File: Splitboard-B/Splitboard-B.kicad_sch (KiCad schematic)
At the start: 86 parts, among them J1 USB_C_Receptacle, K1 KEYSW, K10 KEYSW, K11 KEYSW, K12 KEYSW, K13 KEYSW, K14 KEYSW, K15 KEYSW, K16 KEYSW, K17 KEYSW, K18 KEYSW, K19 KEYSW, K2 KEYSW, K20 KEYSW, K21 KEYSW, K22 KEYSW, K23 KEYSW, K24 KEYSW, K25 KEYSW, K26 KEYSW, K27 KEYSW, K28 KEYSW, K29 KEYSW, K3 KEYSW, K30 KEYSW, K31 KEYSW, K32 KEYSW, K33 KEYSW, K34 KEYSW, K35 KEYSW, K36 KEYSW, K37 KEYSW, K38 KEYSW, K4 KEYSW, K5 KEYSW, K6 KEYSW, K7 KEYSW, K8 KEYSW, K9 KEYSW, SW1 RotaryEncoder, U1 MCP23018-E{slash}SP, U3 CR2013-MI2120

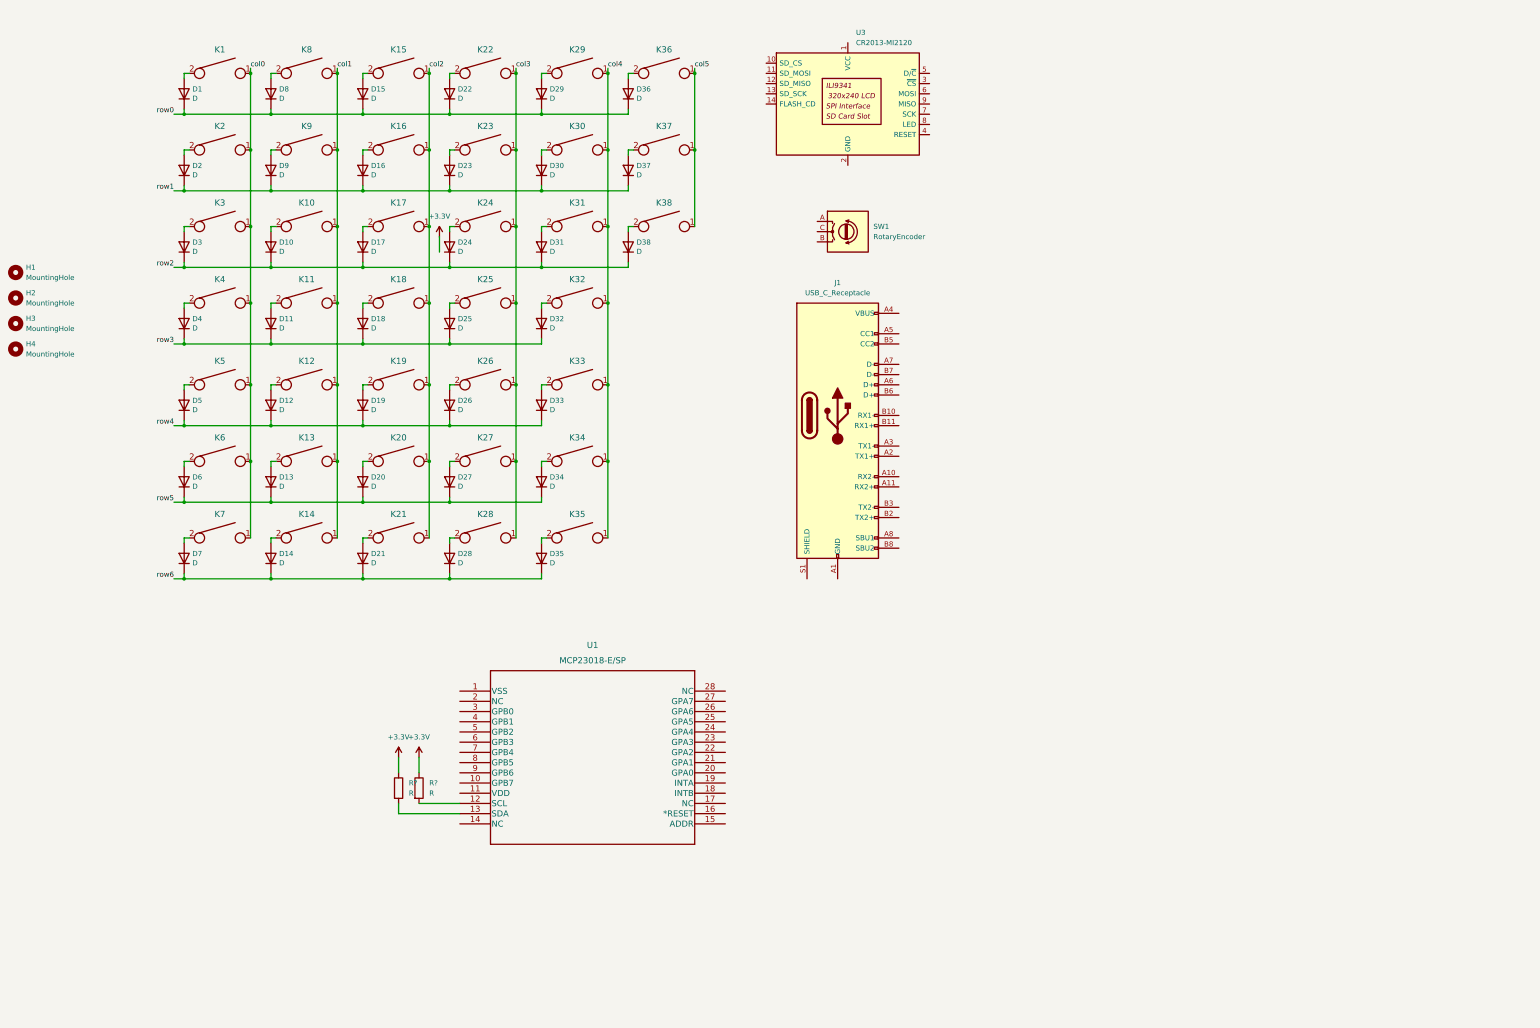
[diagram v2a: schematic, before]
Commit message: Schematic changes, linked both boards under a new project
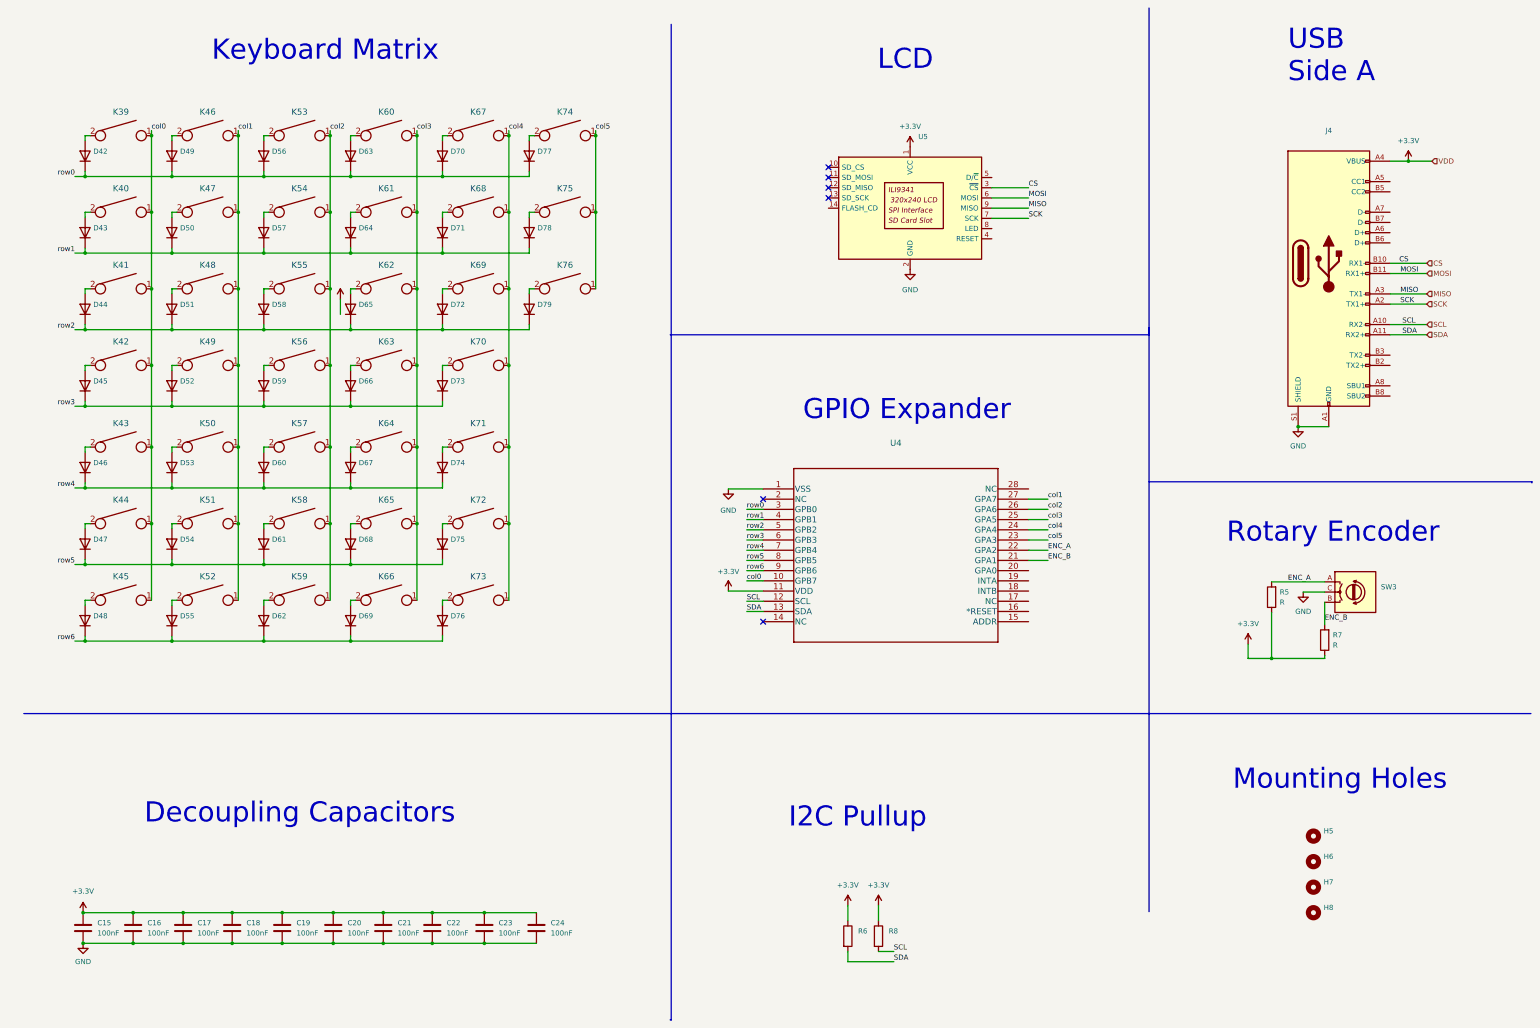
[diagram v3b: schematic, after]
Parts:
- removed D1, D10, D11, D12, D13, D14, D15, D16, D17, D18, D19, D2, D20, D21, D22, D23, D24, D25, D26, D27, D28, D29, D3, D30, D31, D32, D33, D34, D35, D36, D37, D38, D4, D5, D6, D7, D8, D9: D, Diode_SMD:D_SOD-123, symbol KBT1-rescue:D-Device
- removed H1, H2, H3, H4: MountingHole, MountingHole:MountingHole_2.7mm, symbol Mechanical:MountingHole
- removed J1: USB_C_Receptacle, USB_C_Receptacle_GCT_USB4085, symbol Connector:USB_C_Receptacle
- removed K1, K10, K11, K12, K13, K14, K15, K16, K17, K18, K19, K2, K20, K21, K22, K23, K24, K25, K26, K27, K28, K29, K3, K30, K31, K32, K33, K34, K35, K36, K37, K38, K4, K5, K6, K7, K8, K9: KEYSW, 6:SW_Hotswap_Kailh_MX_plated, symbol KBT1-rescue:KEYSW-keyboard_parts
- removed R? (x2): R, symbol Device:R
- removed SW1: RotaryEncoder, Rotary_Encoder:RotaryEncoder_Alps_EC12E_Vertical_H20mm, symbol Device:RotaryEncoder
- removed U3: CR2013-MI2120, Display:CR2013-MI2120, symbol Driver_Display:CR2013-MI2120
- added C15, C16, C17, C18, C19, C20, C21, C22, C23, C24: 100nF, symbol Device:C
- added D42, D43, D44, D45, D46, D47, D48, D49, D50, D51, D52, D53, D54, D55, D56, D57, D58, D59, D60, D61, D62, D63, D64, D65, D66, D67, D68, D69, D70, D71, D72, D73, D74, D75, D76, D77, D78, D79: (no value), symbol KBT1-rescue:D-Device
- added H5, H6, H7, H8: (no value), symbol Mechanical:MountingHole
- added J4: (no value), symbol Connector:USB_C_Receptacle
- added K39, K40, K41, K42, K43, K44, K45, K46, K47, K48, K49, K50, K51, K52, K53, K54, K55, K56, K57, K58, K59, K60, K61, K62, K63, K64, K65, K66, K67, K68, K69, K70, K71, K72, K73, K74, K75, K76: (no value), symbol KBT1-rescue:KEYSW-keyboard_parts
- added R5, R7: R, symbol Device:R
- added R6, R8: ~, symbol Device:R
- added SW3: (no value), symbol Device:RotaryEncoder
- added U5: (no value), symbol Driver_Display:CR2013-MI2120
- U4: renamed from U1; value MCP23018-E/SP -> (none); footprint 6:MCP23018-E&slash_SP -> (none)
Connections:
- net +3.3V: now also U4.11 (VDD), C15.1, C16.1, C17.1, C18.1, C19.1, C20.1, C21.1, C22.1, C23.1, C24.1, J4.A4 (VBUS), J4.A9 (VBUS), J4.B4 (VBUS), J4.B9 (VBUS), R5.1, R6.1, R7.1, R8.1, U5.1 (VCC)
- net col0: now also U4.10 (GPB7), K39.1, K40.1, K41.1, K42.1, K43.1, K44.1, K45.1
- net col1: now also U4.27 (GPA7), K46.1, K47.1, K48.1, K49.1, K50.1, K51.1, K52.1
- net col2: now also U4.26 (GPA6), K53.1, K54.1, K55.1, K56.1, K57.1, K58.1, K59.1
- net col3: now also U4.25 (GPA5), K60.1, K61.1, K62.1, K63.1, K64.1, K65.1, K66.1
- net col4: now also U4.24 (GPA4), K67.1, K68.1, K69.1, K70.1, K71.1, K72.1, K73.1
- net col5: now also U4.23 (GPA3), K74.1, K75.1, K76.1
- net row0: now also U4.3 (GPB0), D42.1 (K), D49.1 (K), D56.1 (K), D63.1 (K), D70.1 (K), D77.1 (K)
- net row1: now also U4.4 (GPB1), D43.1 (K), D50.1 (K), D57.1 (K), D64.1 (K), D71.1 (K), D78.1 (K)
- net row2: now also U4.5 (GPB2), D44.1 (K), D51.1 (K), D58.1 (K), D65.1 (K), D72.1 (K), D79.1 (K)
- net row3: now also U4.6 (GPB3), D45.1 (K), D52.1 (K), D59.1 (K), D66.1 (K), D73.1 (K)
- net row4: now also U4.7 (GPB4), D46.1 (K), D53.1 (K), D60.1 (K), D67.1 (K), D74.1 (K)
- net row5: now also U4.8 (GPB5), D47.1 (K), D54.1 (K), D61.1 (K), D68.1 (K), D75.1 (K)
- net row6: now also U4.9 (GPB6), D48.1 (K), D55.1 (K), D62.1 (K), D69.1 (K), D76.1 (K)
- net GND: now reaches U4.1 (VSS)
- net GND: now also C15.2, C16.2, C17.2, C18.2, C19.2, C20.2, C21.2, C22.2, C23.2, C24.2, J4.A1 (GND), J4.A12 (GND), J4.B1 (GND), J4.B12 (GND), J4.S1 (SHIELD), SW3.C, U5.2 (GND)
- net SCL: now reaches U4.12 (SCL)
- net SCL: now also J4.A10 (RX2-), R8.2
- net SDA: now reaches U4.13 (SDA)
- net SDA: now also J4.A11 (RX2+), R6.2
- net ENC_B: now reaches U4.21 (GPA1)
- net ENC_B: now also R7.2, SW3.B
- net ENC_A: now reaches U4.22 (GPA2)
- net ENC_A: now also R5.2, SW3.A
- new net: D56.2 (A), K53.2
- new net: D51.2 (A), K48.2
- new net: D45.2 (A), K42.2
- new net: D64.2 (A), K61.2
- new net: D65.2 (A), K62.2
- new net: D42.2 (A), K39.2
- new net: D44.2 (A), K41.2
- new net: D58.2 (A), K55.2
- new net: D47.2 (A), K44.2
- new net: D75.2 (A), K72.2
- new net: D49.2 (A), K46.2
- new net: D74.2 (A), K71.2
- new net: D76.2 (A), K73.2
- new net: D62.2 (A), K59.2
- new net: D61.2 (A), K58.2
- new net: D53.2 (A), K50.2
- new net: D78.2 (A), K75.2
- new net: D68.2 (A), K65.2
- new net: D59.2 (A), K56.2
- new net: D70.2 (A), K67.2
- new net: D63.2 (A), K60.2
- new net: D60.2 (A), K57.2
- new net: D69.2 (A), K66.2
- new net: D72.2 (A), K69.2
- new net: D52.2 (A), K49.2
- new net: D46.2 (A), K43.2
- new net: D55.2 (A), K52.2
- new net: D43.2 (A), K40.2
- new net: D54.2 (A), K51.2
- new net: D57.2 (A), K54.2
- new net: D71.2 (A), K68.2
- new net: D79.2 (A), K76.2
- new net: D66.2 (A), K63.2
- new net: D67.2 (A), K64.2
- new net: D50.2 (A), K47.2
- new net: D73.2 (A), K70.2
- new net: D48.2 (A), K45.2
- new net: D77.2 (A), K74.2
- new net CS: J4.B10 (RX1-), U5.3 (~{CS})
- new net MISO: J4.A3 (TX1-), U5.9 (MISO)
- new net MOSI: J4.B11 (RX1+), U5.6 (MOSI)
- new net SCK: J4.A2 (TX1+), U5.7 (SCK)
- no-connect marks 0 -> 6
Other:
- note added: "Decoupling Capacitors"
- note added: "GPIO Expander"
- note added: "I2C Pullup"
- note added: "Keyboard Matrix"
- note added: "LCD"
- note added: "Mounting Holes"
- note added: "Rotary Encoder"
- note added: "USB Side A"
- moved on the sheet: U4

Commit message: Schema changes
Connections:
- no-connect marks 6 -> 8
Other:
- note added: "Splitboard Side B ECE 477 Group 4 Final Project"
- moved on the sheet: R5, R7, SW3, U5

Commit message: Schema changes (rotary encoder, debug header)
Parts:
- added C? (x2): .01uF, symbol Device:C
- added R? (x2): 10k, symbol Device:R
- D42, D43, D44, D45, D46, D47, D48, D49, D50, D51, D52, D53, D54, D55, D56, D57, D58, D59, D60, D61, D62, D63, D64, D65, D66, D67, D68, D69, D70, D71, D72, D73, D74, D75, D76, D77, D78, D79: value (none) -> D; footprint (none) -> Diode_SMD:D_SOD-123
- H5, H6, H7, H8: value (none) -> MountingHole; footprint (none) -> MountingHole:MountingHole_2.7mm
- J4: value (none) -> USB_C_Receptacle; footprint (none) -> USB_C_Receptacle_GCT_USB4085
- K39, K40, K41, K42, K43, K44, K45, K46, K47, K48, K49, K50, K51, K52, K53, K54, K55, K56, K57, K58, K59, K60, K61, K62, K63, K64, K65, K66, K67, K68, K69, K70, K71, K72, K73, K74, K75, K76: value (none) -> KEYSW; footprint (none) -> 6:SW_Hotswap_Kailh_MX_plated
- R5, R7: value R -> 10k
- SW3: value (none) -> RotaryEncoder; footprint (none) -> Rotary_Encoder:RotaryEncoder_Alps_EC12E_Vertical_H20mm; symbol Device:RotaryEncoder -> Device:RotaryEncoder_Switch
- U4: value (none) -> MCP23018-E/SP; footprint (none) -> 6:MCP23018-E&slash_SP
- U5: value (none) -> CR2013-MI2120; footprint (none) -> Display:CR2013-MI2120
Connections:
- net +3.3V: now also R?.1, R?.1; no longer R5.1, R7.1
- net ENC_A: now also R5.1, C?.1; no longer R5.2, SW3.A
- net ENC_B: now also C?.2; no longer SW3.B
- net GND: now also C?.1, C?.2
- new net: R5.2, R?.2, SW3.A
- new net: R7.1, R?.2, SW3.B
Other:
- moved on the sheet: R5, R7

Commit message: updated some pins and net labels on sba
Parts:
- C15, C16, C17, C18, C19, C20, C21, C22, C23, C24: value 100nF -> (none)
- C? (x2): value .01uF -> (none)
- D42, D43, D44, D45, D46, D47, D48, D49, D50, D51, D52, D53, D54, D55, D56, D57, D58, D59, D60, D61, D62, D63, D64, D65, D66, D67, D68, D69, D70, D71, D72, D73, D74, D75, D76, D77, D78, D79: value D -> (none); footprint Diode_SMD:D_SOD-123 -> (none)
- H5, H6, H7, H8: value MountingHole -> (none); footprint MountingHole:MountingHole_2.7mm -> (none)
- J4: value USB_C_Receptacle -> (none); footprint USB_C_Receptacle_GCT_USB4085 -> (none)
- K39, K40, K41, K42, K43, K44, K45, K46, K47, K48, K49, K50, K51, K52, K53, K54, K55, K56, K57, K58, K59, K60, K61, K62, K63, K64, K65, K66, K67, K68, K69, K70, K71, K72, K73, K74, K75, K76: value KEYSW -> (none); footprint 6:SW_Hotswap_Kailh_MX_plated -> (none)
- R5, R7, R? (x2): value 10k -> (none)
- R6, R8: value ~ -> (none)
- SW3: value RotaryEncoder -> (none); footprint Rotary_Encoder:RotaryEncoder_Alps_EC12E_Vertical_H20mm -> (none)
- U5: value CR2013-MI2120 -> (none); footprint Display:CR2013-MI2120 -> (none)
- renumbered U4 to U1

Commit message: Updated Schematics with suggestions from course staff
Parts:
- removed C17, C18, C19, C20, C21, C22, C23, C24, C? (x2): (no value), symbol Device:C
- removed R8, R? (x2): (no value), symbol Device:R
- removed SW3: (no value), symbol Device:RotaryEncoder_Switch
- removed U1: MCP23018-E/SP, 6:MCP23018-E&slash_SP, symbol Interface_Expansion:MCP23018-E{brace}slash}SP
- added C1, C?: 100nF, Capacitor_SMD:C_0805_2012Metric, symbol Device:C
- added C2, C3: .01uF, Capacitor_SMD:C_0805_2012Metric, symbol Device:C
- added C6, C7: 10u, Capacitor_SMD:C_0805_2012Metric, symbol Device:C
- added C?: 10uf, Capacitor_SMD:C_0805_2012Metric, symbol Device:C
- added D39: D_Schottky, Diode_SMD:D_SOD-123, symbol Device:D_Schottky
- added FB1: 100 @ 100 MHz, Resistor_SMD:R_0805_2012Metric, symbol Device:FerriteBead
- added J2: Conn_01x09, Connector_PinHeader_2.54mm:PinHeader_1x09_P2.54mm_Horizontal, symbol Connector_Generic:Conn_01x09
- added R1, R2: 4K7, Resistor_SMD:R_0805_2012Metric, symbol Device:R
- added R3, R4, R? (x6): 10k, Resistor_SMD:R_0805_2012Metric, symbol Device:R
- added R? (x23): 20, Resistor_SMD:R_0805_2012Metric, symbol Device:R
- added SW1: RotaryEncoder, Rotary_Encoder:RotaryEncoder_Alps_EC11E-Switch_Vertical_H20mm, symbol Device:RotaryEncoder_Switch
- added U2: MCP23017_SP, Package_DIP:DIP-28_W7.62mm, symbol Interface_Expansion:MCP23017_SP
- added U3: AMS1117-3.3, Package_TO_SOT_SMD:SOT-223-3_TabPin2, symbol Regulator_Linear:AMS1117-3.3
- C4: renamed from C15; value (none) -> 100nF; footprint (none) -> Capacitor_SMD:C_0805_2012Metric
- C5: renamed from C16; value (none) -> 100nF; footprint (none) -> Capacitor_SMD:C_0805_2012Metric
- D1: renamed from D42; value (none) -> D; footprint (none) -> Diode_SMD:D_SOD-123
- D10: renamed from D51; value (none) -> D; footprint (none) -> Diode_SMD:D_SOD-123
- D11: renamed from D52; value (none) -> D; footprint (none) -> Diode_SMD:D_SOD-123
- D12: renamed from D53; value (none) -> D; footprint (none) -> Diode_SMD:D_SOD-123
- D13: renamed from D54; value (none) -> D; footprint (none) -> Diode_SMD:D_SOD-123
- D14: renamed from D55; value (none) -> D; footprint (none) -> Diode_SMD:D_SOD-123
- D15: renamed from D56; value (none) -> D; footprint (none) -> Diode_SMD:D_SOD-123
- D16: renamed from D57; value (none) -> D; footprint (none) -> Diode_SMD:D_SOD-123
- D17: renamed from D58; value (none) -> D; footprint (none) -> Diode_SMD:D_SOD-123
- D18: renamed from D59; value (none) -> D; footprint (none) -> Diode_SMD:D_SOD-123
- D19: renamed from D60; value (none) -> D; footprint (none) -> Diode_SMD:D_SOD-123
- D2: renamed from D43; value (none) -> D; footprint (none) -> Diode_SMD:D_SOD-123
- D20: renamed from D61; value (none) -> D; footprint (none) -> Diode_SMD:D_SOD-123
- D21: renamed from D62; value (none) -> D; footprint (none) -> Diode_SMD:D_SOD-123
- D22: renamed from D63; value (none) -> D; footprint (none) -> Diode_SMD:D_SOD-123
- D23: renamed from D64; value (none) -> D; footprint (none) -> Diode_SMD:D_SOD-123
- D24: renamed from D65; value (none) -> D; footprint (none) -> Diode_SMD:D_SOD-123
- D25: renamed from D66; value (none) -> D; footprint (none) -> Diode_SMD:D_SOD-123
- D26: renamed from D67; value (none) -> D; footprint (none) -> Diode_SMD:D_SOD-123
- D27: renamed from D68; value (none) -> D; footprint (none) -> Diode_SMD:D_SOD-123
- D28: renamed from D69; value (none) -> D; footprint (none) -> Diode_SMD:D_SOD-123
- D29: renamed from D70; value (none) -> D; footprint (none) -> Diode_SMD:D_SOD-123
- D3: renamed from D44; value (none) -> D; footprint (none) -> Diode_SMD:D_SOD-123
- D30: renamed from D71; value (none) -> D; footprint (none) -> Diode_SMD:D_SOD-123
- D31: renamed from D72; value (none) -> D; footprint (none) -> Diode_SMD:D_SOD-123
- D32: renamed from D73; value (none) -> D; footprint (none) -> Diode_SMD:D_SOD-123
- D33: renamed from D74; value (none) -> D; footprint (none) -> Diode_SMD:D_SOD-123
- D34: renamed from D75; value (none) -> D; footprint (none) -> Diode_SMD:D_SOD-123
- D35: renamed from D76; value (none) -> D; footprint (none) -> Diode_SMD:D_SOD-123
- D36: renamed from D77; value (none) -> D; footprint (none) -> Diode_SMD:D_SOD-123
- D37: renamed from D78; value (none) -> D; footprint (none) -> Diode_SMD:D_SOD-123
- D38: renamed from D79; value (none) -> D; footprint (none) -> Diode_SMD:D_SOD-123
- D4: renamed from D45; value (none) -> D; footprint (none) -> Diode_SMD:D_SOD-123
- D5: renamed from D46; value (none) -> D; footprint (none) -> Diode_SMD:D_SOD-123
- D6: renamed from D47; value (none) -> D; footprint (none) -> Diode_SMD:D_SOD-123
- D7: renamed from D48; value (none) -> D; footprint (none) -> Diode_SMD:D_SOD-123
- D8: renamed from D49; value (none) -> D; footprint (none) -> Diode_SMD:D_SOD-123
- D9: renamed from D50; value (none) -> D; footprint (none) -> Diode_SMD:D_SOD-123
- H1: renamed from H5; value (none) -> MountingHole; footprint (none) -> MountingHole:MountingHole_2.7mm
- H2: renamed from H6; value (none) -> MountingHole; footprint (none) -> MountingHole:MountingHole_2.7mm
- H3: renamed from H7; value (none) -> MountingHole; footprint (none) -> MountingHole:MountingHole_2.7mm
- H4: renamed from H8; value (none) -> MountingHole; footprint (none) -> MountingHole:MountingHole_2.7mm
- J1: renamed from J4; value (none) -> USB_C_Receptacle; footprint (none) -> Connector_USB:USB_C_Receptacle_Amphenol_12401548E4-2A
- K1: renamed from K39; value (none) -> KEYSW; footprint (none) -> 6:SW_Hotswap_Kailh_MX_plated
- K10: renamed from K48; value (none) -> KEYSW; footprint (none) -> 6:SW_Hotswap_Kailh_MX_plated
- K11: renamed from K49; value (none) -> KEYSW; footprint (none) -> 6:SW_Hotswap_Kailh_MX_plated
- K12: renamed from K50; value (none) -> KEYSW; footprint (none) -> 6:SW_Hotswap_Kailh_MX_plated
- K13: renamed from K51; value (none) -> KEYSW; footprint (none) -> 6:SW_Hotswap_Kailh_MX_plated
- K14: renamed from K52; value (none) -> KEYSW; footprint (none) -> 6:SW_Hotswap_Kailh_MX_plated
- K15: renamed from K53; value (none) -> KEYSW; footprint (none) -> 6:SW_Hotswap_Kailh_MX_plated
- K16: renamed from K54; value (none) -> KEYSW; footprint (none) -> 6:SW_Hotswap_Kailh_MX_plated
- K17: renamed from K55; value (none) -> KEYSW; footprint (none) -> 6:SW_Hotswap_Kailh_MX_plated
- K18: renamed from K56; value (none) -> KEYSW; footprint (none) -> 6:SW_Hotswap_Kailh_MX_plated
- K19: renamed from K57; value (none) -> KEYSW; footprint (none) -> 6:SW_Hotswap_Kailh_MX_plated
- K2: renamed from K40; value (none) -> KEYSW; footprint (none) -> 6:SW_Hotswap_Kailh_MX_plated
- K20: renamed from K58; value (none) -> KEYSW; footprint (none) -> 6:SW_Hotswap_Kailh_MX_plated
- K21: renamed from K59; value (none) -> KEYSW; footprint (none) -> 6:SW_Hotswap_Kailh_MX_plated
- K22: renamed from K60; value (none) -> KEYSW; footprint (none) -> 6:SW_Hotswap_Kailh_MX_plated
- K23: renamed from K61; value (none) -> KEYSW; footprint (none) -> 6:SW_Hotswap_Kailh_MX_plated
- K24: renamed from K62; value (none) -> KEYSW; footprint (none) -> 6:SW_Hotswap_Kailh_MX_plated
- K25: renamed from K63; value (none) -> KEYSW; footprint (none) -> 6:SW_Hotswap_Kailh_MX_plated
- K26: renamed from K64; value (none) -> KEYSW; footprint (none) -> 6:SW_Hotswap_Kailh_MX_plated
- K27: renamed from K65; value (none) -> KEYSW; footprint (none) -> 6:SW_Hotswap_Kailh_MX_plated
- K28: renamed from K66; value (none) -> KEYSW; footprint (none) -> 6:SW_Hotswap_Kailh_MX_plated
- K29: renamed from K67; value (none) -> KEYSW; footprint (none) -> 6:SW_Hotswap_Kailh_MX_plated
- K3: renamed from K41; value (none) -> KEYSW; footprint (none) -> 6:SW_Hotswap_Kailh_MX_plated
- K30: renamed from K68; value (none) -> KEYSW; footprint (none) -> 6:SW_Hotswap_Kailh_MX_plated
- K31: renamed from K69; value (none) -> KEYSW; footprint (none) -> 6:SW_Hotswap_Kailh_MX_plated
- K32: renamed from K70; value (none) -> KEYSW; footprint (none) -> 6:SW_Hotswap_Kailh_MX_plated
- K33: renamed from K71; value (none) -> KEYSW; footprint (none) -> 6:SW_Hotswap_Kailh_MX_plated
- K34: renamed from K72; value (none) -> KEYSW; footprint (none) -> 6:SW_Hotswap_Kailh_MX_plated
- K35: renamed from K73; value (none) -> KEYSW; footprint (none) -> 6:SW_Hotswap_Kailh_MX_plated
- K36: renamed from K74; value (none) -> KEYSW; footprint (none) -> 6:SW_Hotswap_Kailh_MX_plated
- K37: renamed from K75; value (none) -> KEYSW; footprint (none) -> 6:SW_Hotswap_Kailh_MX_plated
- K38: renamed from K76; value (none) -> KEYSW; footprint (none) -> 6:SW_Hotswap_Kailh_MX_plated
- K4: renamed from K42; value (none) -> KEYSW; footprint (none) -> 6:SW_Hotswap_Kailh_MX_plated
- K5: renamed from K43; value (none) -> KEYSW; footprint (none) -> 6:SW_Hotswap_Kailh_MX_plated
- K6: renamed from K44; value (none) -> KEYSW; footprint (none) -> 6:SW_Hotswap_Kailh_MX_plated
- K7: renamed from K45; value (none) -> KEYSW; footprint (none) -> 6:SW_Hotswap_Kailh_MX_plated
- K8: renamed from K46; value (none) -> KEYSW; footprint (none) -> 6:SW_Hotswap_Kailh_MX_plated
- K9: renamed from K47; value (none) -> KEYSW; footprint (none) -> 6:SW_Hotswap_Kailh_MX_plated
- R5, R6, R7: value (none) -> 10k; footprint (none) -> Resistor_SMD:R_0805_2012Metric
- U1: renamed from U5; value (none) -> CR2013-MI2120; footprint (none) -> Display:CR2013-MI2120
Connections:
- net +3.3V: now also U1.8 (LED), C7.1, J2.1 (Pin_1), R1.1, R2.1, R3.2, R4.1, R?.2, R?.2, R?.2, R?.2, R?.2, R?.2, U2.18 (~{RESET}), U2.9 (VDD), U3.2 (VO); no longer J1.A4 (VBUS), J1.A9 (VBUS), J1.B4 (VBUS), J1.B9 (VBUS), U1.1 (VCC)
- net ENC_A: now also C2.1, R?.1
- net ENC_B: now also C3.2, R?.1
- net GND: now also C1.1, C2.2, C3.1, C6.2, C7.2, C?.2, C?.2, J2.9 (Pin_9), SW1.C, SW1.S2, U2.10 (VSS), U2.15 (A0), U2.16 (A1), U2.17 (A2), U3.1 (GND)
- net MOSI: now also J2.7 (Pin_7), R?.1; no longer J1.B11 (RX1+)
- net SCK: now also J2.8 (Pin_8), R?.1; no longer J1.A2 (TX1+)
- net SCL: now also J2.2 (Pin_2), R2.2, R?.1, U2.13 (SDA); no longer J1.A10 (RX2-)
- net SDA: now also J2.3 (Pin_3), R1.2, R?.1, U2.12 (SCK); no longer J1.A11 (RX2+), R6.2
- net col0: now also R?.1
- net col1: now also R?.1
- net col2: now also R?.1
- net col3: now also R?.1
- net col4: now also R?.1
- net col5: now also R?.1
- net row0: now also R?.1
- net row1: now also R?.1
- net row2: now also R?.1
- net row3: now also R?.1
- net row4: now also R?.1
- net row5: now also R?.1
- net row6: now also R?.1
- net at J1.A5 (CC1): now also J1.B5 (CC2), R?.2
- net at J1.A6 (D+): now also J1.B6 (D+), R?.2
- net at J1.A7 (D-): now also J1.B7 (D-), R?.2
- net at J1.A8 (SBU1): now also J1.B8 (SBU2), R?.2
- net at J1.B2 (TX2+): now also J1.A2 (TX1+)
- net at J1.B3 (TX2-): now also J1.A3 (TX1-), R?.2
- net at R5.2: now also R4.2, SW1.A
- net at R7.1: now also R6.2, SW1.B
- net LCD2_RST: now reaches U1.4 (RESET)
- net LCD2_RST: now also J2.6 (Pin_6), R?.1
- net LCD2_DC: now reaches U1.5 (D/~{C})
- net LCD2_DC: now also J2.5 (Pin_5), R?.1
- net CS: no longer names the net of J1.B10 (RX1-)
- net CS: now also J1.A10 (RX2-), R?.2; no longer U1.3 (~{CS})
- net MISO: no longer names the net of U1.9 (MISO)
- net MISO: no longer J1.A3 (TX1-)
- new net: J1.A11 (RX2+), J1.B11 (RX1+), R?.2
- new net: R?.2, U2.3 (GPB2)
- new net: R?.1, R?.2, U2.21 (GPA0)
- new net: R?.1, R?.2, U2.22 (GPA1)
- new net: R?.1, R?.2, U2.24 (GPA3)
- new net: R?.2, U2.7 (GPB6)
- new net: C6.1, FB1.2, U3.3 (VI)
- new net: R?.2, U2.1 (GPB0)
- new net: R?.2, U2.2 (GPB1)
- new net: R?.1, R?.2, U2.23 (GPA2)
- new net: R?.1, R?.2, U2.25 (GPA4)
- new net: R?.1, R?.2, U2.26 (GPA5)
- new net: R?.2, U2.27 (GPA6)
- new net: R?.2, U2.28 (GPA7)
- new net: R?.2, U2.4 (GPB3)
- new net: R?.2, U2.5 (GPB4)
- new net: R?.2, U2.6 (GPB5)
- new net: R?.2, U2.8 (GPB7)
- new net: D39.1 (K), FB1.1
- new net ENC_SW: C1.2, R3.1, R?.1, SW1.S1
- new net LCD2_CS: J2.4 (Pin_4), R?.1, U1.3 (~{CS})
- new net VBUS: C?.1, C?.1, D39.2 (A), J1.A4 (VBUS), J1.A9 (VBUS), J1.B4 (VBUS), J1.B9 (VBUS), U1.1 (VCC)
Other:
- note added: "Debugging Header"
- note added: "From MCP23017 datasheet: GPA7 & GPB7 are output only"
- note added: "I don't know what this circuit is going to look like yet"
- note added: "Pooling Caps"
- note added: "USB-C Side A"
- note added: "Voltage Regulator"
- note removed: "I2C Pullup"
- note removed: "USB Side A"
- moved on the sheet: C4, C5, D1, D10, D11, D12, D13, D14, D15, D16, D17, D18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

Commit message: Layout changes
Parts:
- gave numbers to parts that had none: 31
